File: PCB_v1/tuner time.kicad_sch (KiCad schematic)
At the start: 0 parts

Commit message: changed debouncing order, switches to jst, and array resistors
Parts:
- added J9: Conn_01x03, symbol Connector_Generic:Conn_01x03
- added U3: C1F 2, C1_BEL, symbol GT_LIbrary:C1F_2
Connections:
- net GND: now also J9.3 (Pin_3)
- new net MCU_RX: J9.1 (Pin_1)
- new net MCU_TX: J9.2 (Pin_2)

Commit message: PCB changes before changing Seth's clock
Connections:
- net 5V: now also U3.1
- net Motor/VMOT: now also U3.2
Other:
- sheet Motor ports: added none; removed CFG, GND
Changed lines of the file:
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@@
+	(wire
+		(pts
+			(xy 163.83 95.25) (xy 158.75 95.25)
+		)
+		(stroke
+			(width 0)
+			(type default)
+		)
+	)
 	(wire
 		(pts
@@
 	(wire
 		(pts
+			(xy 181.61 97.79) (xy 154.94 97.79)
+		)
+		(stroke
+			(width 0)
+			(type default)
+		)
+	)
+	(wire
+		(pts
 			(xy 182.88 139.7) (xy 166.37 139.7)
 		)
@@
 	(wire
 		(pts
+			(xy 173.99 95.25) (xy 181.61 95.25)
+		)
+		(stroke
+			(width 0)
+			(type default)
+		)
+	)
+	(wire
+		(pts
 			(xy 86.36 134.62) (xy 73.66 134.62)
 		)
@@
 	(wire
 		(pts
+			(xy 154.94 97.79) (xy 154.94 96.52)
+		)
+		(stroke
+			(width 0)
+			(type default)
+		)
+	)
+	(wire
+		(pts
 			(xy 209.55 138.43) (xy 219.71 138.43)
 		)
@@
 		(pts
 			(xy 182.88 144.78) (xy 166.37 144.78)
+		)
+		(stroke
+			(width 0)
+			(type default)
+		)
+	)
+	(wire
+		(pts
+			(xy 158.75 95.25) (xy 158.75 91.44)
 		)
 		(stroke
@@
 	)
 	(symbol
+		(lib_id "power:VCC")
+		(at 154.94 96.52 0)
+		(unit 1)
+		(exclude_from_sim no)
+		(in_bom yes)
+		(on_board yes)
+		(dnp no)
+		(property "Reference" "#PWR075"
+			(at 154.94 100.33 0)
+			(effects
+				(font
+					(size 1.27 1.27)
+				)
+				(hide yes)
+			)
+		)
+		(property "Value" "3V3"
+			(at 154.94 92.71 0)
+			(effects
+				(font
+					(size 1.27 1.27)
+				)
+			)
+		)
+		(property "Footprint" ""
+			(at 154.94 96.52 0)
+			(effects
+				(font
+					(size 1.27 1.27)
+				)
+				(hide yes)
+			)
+		)
+		(property "Datasheet" ""
+			(at 154.94 96.52 0)
+			(effects
+				(font
+					(size 1.27 1.27)
+				)
+				(hide yes)
+			)
+		)
+		(property "Description" "Power symbol creates a global label with name \"VCC\""
+			(at 154.94 96.52 0)
+			(effects
+				(font
+					(size 1.27 1.27)
+				)
+				(hide yes)
+			)
+		)
+		(pin "1"
+		)
+		(instances
+			(project "tuner time"
+				(path "/353cef6a-fb6e-40d9-89f8-eb54b7aa5118"
+					(reference "#PWR075")
+					(unit 1)
+				)
+			)
+		)
+	)
+	(symbol
 		(lib_id "power:GND")
 		(at 214.63 154.94 0)
@@
 				(path "/353cef6a-fb6e-40d9-89f8-eb54b7aa5118"
 					(reference "#PWR011")
+					(unit 1)
+				)
+			)
+		)
+	)
+	(symbol
+		(lib_id "power:VCC")
+		(at 158.75 91.44 0)
+		(unit 1)
+		(exclude_from_sim no)
+		(in_bom yes)
+		(on_board yes)
+		(dnp no)
+		(property "Reference" "#PWR074"
+			(at 158.75 95.25 0)
+			(effects
+				(font
+					(size 1.27 1.27)
+				)
+				(hide yes)
+			)
+		)
+		(property "Value" "5V"
+			(at 158.75 87.63 0)
+			(effects
+				(font
+					(size 1.27 1.27)
+				)
+			)
+		)
+		(property "Footprint" ""
+			(at 158.75 91.44 0)
+			(effects
+				(font
+					(size 1.27 1.27)
+				)
+				(hide yes)
+			)
+		)
+		(property "Datasheet" ""
+			(at 158.75 91.44 0)
+			(effects
+				(font
+					(size 1.27 1.27)
+				)
+				(hide yes)
+			)
+		)
+		(property "Description" "Power symbol creates a global label with name \"VCC\""
+			(at 158.75 91.44 0)
+			(effects
+				(font
+					(size 1.27 1.27)
+				)
+				(hide yes)
+			)
+		)
+		(pin "1"
+		)
+		(instances
+			(project "tuner time"
+				(path "/353cef6a-fb6e-40d9-89f8-eb54b7aa5118"
+					(reference "#PWR074")
 					(unit 1)
 				)
@@
 			)
 		)
-		(pin "GND" input
-			(at 181.61 102.87 180)
-			(effects
-				(font
-					(size 1.27 1.27)
-				)
-				(justify left)
-			)
-		)
-		(pin "CFG" input
-			(at 209.55 109.22 0)
-			(effects
-				(font
-					(size 1.27 1.27)
-				)
-				(justify right)
-			)
-		)

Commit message: Update before adding AGND for the power delivery
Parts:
- renumbered J9 to J1, U3 to U1
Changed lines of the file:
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@@
 		(dnp no)
 		(fields_autoplaced yes)
-		(property "Reference" "#PWR05"
+		(property "Reference" "#PWR06"
 			(at 82.55 151.13 0)
 			(effects
@@
 			(project "tuner time"
 				(path "/353cef6a-fb6e-40d9-89f8-eb54b7aa5118"
-					(reference "#PWR05")
+					(reference "#PWR06")
 					(unit 1)
 				)
@@
 		(on_board yes)
 		(dnp no)
-		(property "Reference" "#PWR06"
+		(property "Reference" "#PWR07"
 			(at 154.94 34.29 0)
 			(effects
@@
 			(project "tuner time"
 				(path "/353cef6a-fb6e-40d9-89f8-eb54b7aa5118"
-					(reference "#PWR06")
+					(reference "#PWR07")
 					(unit 1)
 				)
@@
 		(dnp no)
 		(fields_autoplaced yes)
-		(property "Reference" "U3"
+		(property "Reference" "U1"
 			(at 168.91 88.9 0)
 			(effects
@@
 			(project ""
 				(path "/353cef6a-fb6e-40d9-89f8-eb54b7aa5118"
-					(reference "U3")
+					(reference "U1")
 					(unit 1)
 				)
@@
 		(on_board yes)
 		(dnp no)
-		(property "Reference" "#PWR01"
+		(property "Reference" "#PWR02"
 			(at 73.66 135.89 0)
 			(effects
@@
 			(project "tuner time"
 				(path "/353cef6a-fb6e-40d9-89f8-eb54b7aa5118"
-					(reference "#PWR01")
+					(reference "#PWR02")
 					(unit 1)
 				)
@@
 		(dnp no)
 		(fields_autoplaced yes)
-		(property "Reference" "#PWR08"
+		(property "Reference" "#PWR011"
 			(at 160.02 48.26 0)
 			(effects
@@
 			(project "tuner time"
 				(path "/353cef6a-fb6e-40d9-89f8-eb54b7aa5118"
-					(reference "#PWR08")
+					(reference "#PWR011")
 					(unit 1)
 				)
@@
 		(on_board yes)
 		(dnp no)
-		(property "Reference" "#PWR04"
+		(property "Reference" "#PWR05"
 			(at 80.01 132.08 0)
 			(effects
@@
 			(project "tuner time"
 				(path "/353cef6a-fb6e-40d9-89f8-eb54b7aa5118"
-					(reference "#PWR04")
+					(reference "#PWR05")
 					(unit 1)
 				)
@@
 		(dnp no)
 		(fields_autoplaced yes)
-		(property "Reference" "#PWR019"
+		(property "Reference" "#PWR01"
 			(at 36.83 175.26 0)
 			(effects
@@
 			(project "tuner time"
 				(path "/353cef6a-fb6e-40d9-89f8-eb54b7aa5118"
-					(reference "#PWR019")
+					(reference "#PWR01")
 					(unit 1)
 				)
@@
 		(on_board yes)
 		(dnp no)
-		(property "Reference" "#PWR075"
+		(property "Reference" "#PWR08"
 			(at 154.94 100.33 0)
 			(effects
@@
 			(project "tuner time"
 				(path "/353cef6a-fb6e-40d9-89f8-eb54b7aa5118"
-					(reference "#PWR075")
+					(reference "#PWR08")
 					(unit 1)
 				)
@@
 		(dnp no)
 		(fields_autoplaced yes)
-		(property "Reference" "#PWR011"
+		(property "Reference" "#PWR012"
 			(at 214.63 161.29 0)
 			(effects
@@
 			(project "tuner time"
 				(path "/353cef6a-fb6e-40d9-89f8-eb54b7aa5118"
-					(reference "#PWR011")
+					(reference "#PWR012")
 					(unit 1)
 				)
@@
 		(on_board yes)
 		(dnp no)
-		(property "Reference" "#PWR074"
+		(property "Reference" "#PWR09"
 			(at 158.75 95.25 0)
 			(effects
@@
 			(project "tuner time"
 				(path "/353cef6a-fb6e-40d9-89f8-eb54b7aa5118"
-					(reference "#PWR074")
+					(reference "#PWR09")
 					(unit 1)
 				)
@@
 		(dnp no)
 		(fields_autoplaced yes)
-		(property "Reference" "#PWR0107"
+		(property "Reference" "#PWR015"
 			(at 267.97 45.72 0)
 			(effects
@@
 			(project "tuner time"
 				(path "/353cef6a-fb6e-40d9-89f8-eb54b7aa5118"
-					(reference "#PWR0107")
+					(reference "#PWR015")
 					(unit 1)
 				)
@@
 		(dnp no)
 		(fields_autoplaced yes)
-		(property "Reference" "J9"
+		(property "Reference" "J1"
 			(at 29.21 154.94 0)
 			(effects
@@
 			(project ""
 				(path "/353cef6a-fb6e-40d9-89f8-eb54b7aa5118"
-					(reference "J9")
+					(reference "J1")
 					(unit 1)
 				)
@@
 		(on_board yes)
 		(dnp no)
-		(property "Reference" "#PWR012"
+		(property "Reference" "#PWR013"
 			(at 214.63 146.05 0)
 			(effects
@@
 			(project "tuner time"
 				(path "/353cef6a-fb6e-40d9-89f8-eb54b7aa5118"
-					(reference "#PWR012")
+					(reference "#PWR013")
 					(unit 1)
 				)
@@
 		(on_board yes)
 		(dnp no)
-		(property "Reference" "#PWR013"
+		(property "Reference" "#PWR014"
 			(at 219.71 148.59 0)
 			(effects
@@
 			(project "tuner time"
 				(path "/353cef6a-fb6e-40d9-89f8-eb54b7aa5118"
-					(reference "#PWR013")
+					(reference "#PWR014")
 					(unit 1)
 				)
@@
 		(dnp no)
 		(fields_autoplaced yes)
-		(property "Reference" "#PWR03"
+		(property "Reference" "#PWR04"
 			(at 80.01 82.55 0)
 			(effects
@@
 			(project "tuner time"
 				(path "/353cef6a-fb6e-40d9-89f8-eb54b7aa5118"
-					(reference "#PWR03")
+					(reference "#PWR04")
 					(unit 1)
 				)
@@
 		(on_board yes)
 		(dnp no)
-		(property "Reference" "#PWR02"
+		(property "Reference" "#PWR03"
 			(at 80.01 64.77 0)
 			(effects
@@
 			(project "tuner time"
 				(path "/353cef6a-fb6e-40d9-89f8-eb54b7aa5118"
-					(reference "#PWR02")
+					(reference "#PWR03")
 					(unit 1)
 				)
@@
 		(on_board yes)
 		(dnp no)
-		(property "Reference" "#PWR07"
+		(property "Reference" "#PWR010"
 			(at 160.02 30.48 0)
 			(effects
@@
 			(project "tuner time"
 				(path "/353cef6a-fb6e-40d9-89f8-eb54b7aa5118"
-					(reference "#PWR07")
-					(unit 1)
-				)
+					(reference "#PWR010")
+					(unit 1)
+				)

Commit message: Initial placement draft
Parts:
- removed J1: Conn_01x03, symbol Connector_Generic:Conn_01x03
- added D1, D6: Green, LED_SMD:LED_0805_2012Metric_Pad1.15x1.40mm_HandSolder, symbol Device:LED
- added D7: Orange, LED_SMD:LED_0805_2012Metric_Pad1.15x1.40mm_HandSolder, symbol Device:LED
- added JP1: M1, Jumper:SolderJumper-3_P1.3mm_Open_RoundedPad1.0x1.5mm, symbol Jumper:SolderJumper_3_Open
- added JP2: M2, Jumper:SolderJumper-3_P1.3mm_Open_RoundedPad1.0x1.5mm, symbol Jumper:SolderJumper_3_Open
- added JP3: SLP, Jumper:SolderJumper-3_P1.3mm_Bridged12_RoundedPad1.0x1.5mm, symbol Jumper:SolderJumper_3_Bridged12
- added R1: 680, Resistor_SMD:R_0805_2012Metric, symbol Device:R_US
- added R31, R32: 680, Resistor_SMD:R_0805_2012Metric, symbol Device:R
- added TP1, TP2: ~, TestPoint:TestPoint_THTPad_D1.0mm_Drill0.5mm, symbol Connector:TestPoint
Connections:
- net 3V3: now also D6.2 (A)
- net 5V: now also D7.2 (A), JP1.1 (A), JP2.1 (A), JP3.1 (A)
- net GND: now also JP1.3 (B), JP2.3 (B), JP3.3 (B), R1.2, R31.1, R32.1
- net Motor/EN: now also TP2.1
- net Motor/FLT: now also D1.2 (A)
- net Motor/M0: now also JP2.2 (C)
- net Motor/M1: now also JP1.2 (C)
- net Motor/SLP: now also JP3.2 (C)
- net Motor/VREF: now also TP1.1
- new net: D7.1 (K), R31.2
- new net: D6.1 (K), R32.2
- new net: D1.1 (K), R1.1
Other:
- sheet MCU ports: added DIR, I2S2_CLK, I2S2_SD, I2S2_WS, STEP, UART2_RX, UART2_TX; removed none
- sheet Motor ports: added AGND; removed none
- sheet Power Delivery ports: added AGND; removed none
- moved on the sheet: U1

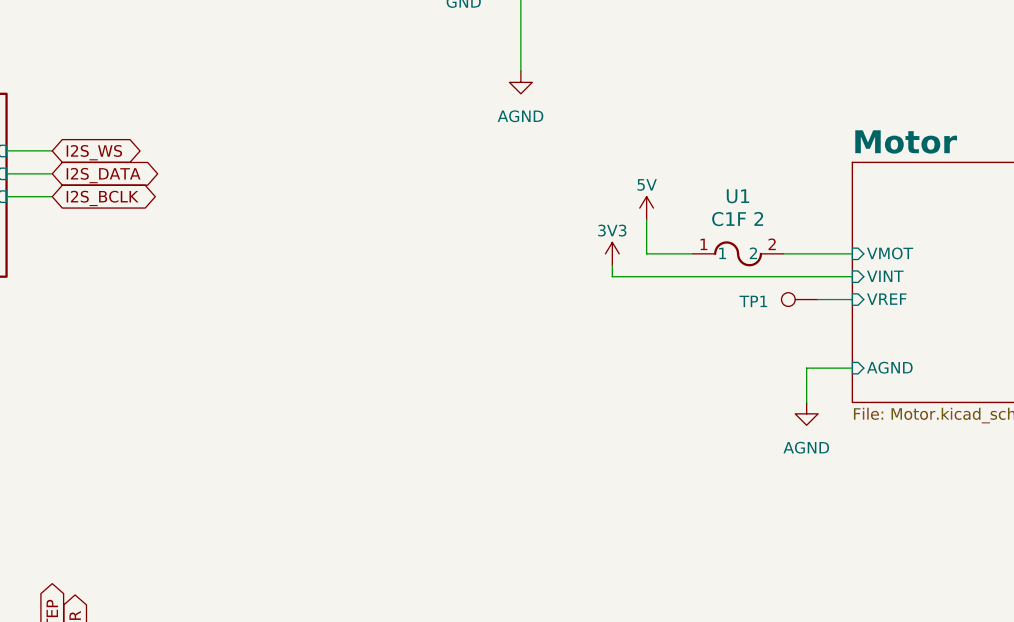
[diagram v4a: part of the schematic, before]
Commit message: updated the schematic only
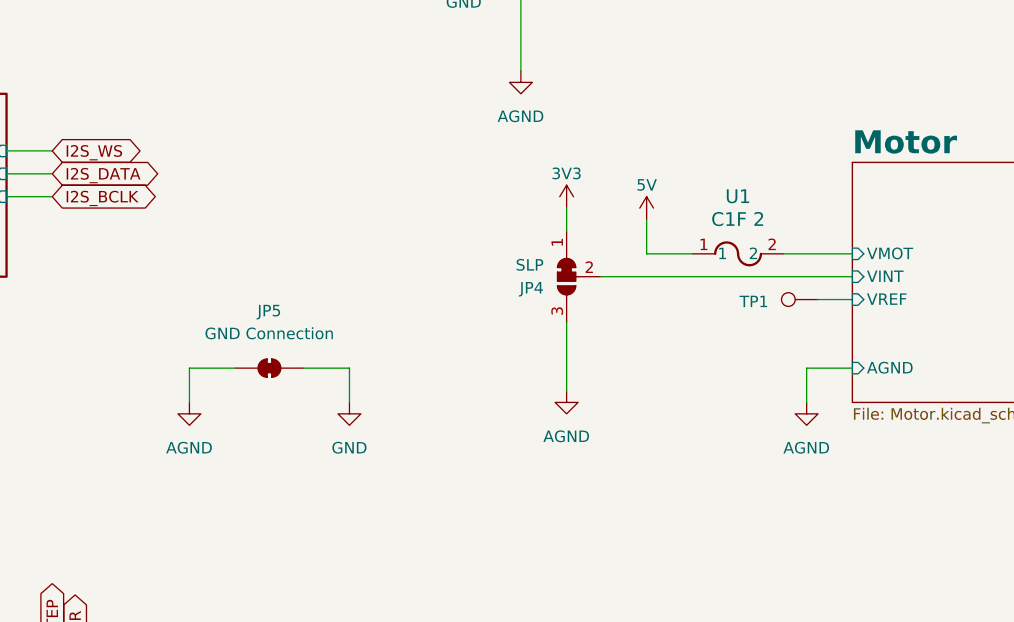
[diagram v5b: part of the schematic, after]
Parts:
- added JP4: SLP, Jumper:SolderJumper-3_P1.3mm_Bridged12_RoundedPad1.0x1.5mm, symbol Jumper:SolderJumper_3_Bridged12
- added JP5: GND Connection, symbol Jumper:SolderJumper_2_Bridged
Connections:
- net 3V3: now also JP4.1 (A)
- net AGND: now also JP4.3 (B), JP5.1 (A)
- net GND: now also JP5.2 (B)
- new net Motor/VINT: JP4.2 (C)
